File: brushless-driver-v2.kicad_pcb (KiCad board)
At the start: 2 copper layers, 86.5 x 63 mm, 37 parts, among them J1 Conn_01x07_Socket, J2 encoder, J3 motor, U5 L7805

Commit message: Started on second power stage, broke first power stage
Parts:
- added C12: 100n, Capacitor_SMD:C_0805_2012Metric_Pad1.18x1.45mm_HandSolder, F.Cu at (247.3, 37.5)
- added C13: 100n, Capacitor_SMD:C_0805_2012Metric_Pad1.18x1.45mm_HandSolder, F.Cu at (247.3, 40.5)
- added C14: 100n, Capacitor_SMD:C_0805_2012Metric_Pad1.18x1.45mm_HandSolder, F.Cu at (247.3, 43.5)
- added IC_A2: IFX007T, meiBib:TO-263-7_TabPin4, F.Cu at (142.5, 38.3)
- added IC_B2: IFX007T, meiBib:TO-263-7_TabPin4, F.Cu at (142.5, 50.6)
- added IC_C2: IFX007T, meiBib:TO-263-7_TabPin4, F.Cu at (142.5, 63.0)
- added J4: motor, TerminalBlock:TerminalBlock_MaiXu_MX126-5.0-03P_1x03_P5.00mm, F.Cu at (234.7, 30.9)
- added R13: 10k, Resistor_SMD:R_0805_2012Metric_Pad1.20x1.40mm_HandSolder, F.Cu at (233.0, 37.5)
- added R14: 10k, Resistor_SMD:R_0805_2012Metric_Pad1.20x1.40mm_HandSolder, F.Cu at (233.0, 40.5)
- added R15: 10k, Resistor_SMD:R_0805_2012Metric_Pad1.20x1.40mm_HandSolder, F.Cu at (233.0, 43.4)
- added R16: 10k, Resistor_SMD:R_0805_2012Metric_Pad1.20x1.40mm_HandSolder, F.Cu at (233.0, 46.4)
- added R17: 5k6, Resistor_SMD:R_0805_2012Metric_Pad1.20x1.40mm_HandSolder, F.Cu at (237.8, 37.5)
- added R18: 5k6, Resistor_SMD:R_0805_2012Metric_Pad1.20x1.40mm_HandSolder, F.Cu at (237.8, 40.5)
- added R19: 10k, Resistor_SMD:R_0805_2012Metric_Pad1.20x1.40mm_HandSolder, F.Cu at (237.8, 43.4)
- added R20: 10k, Resistor_SMD:R_0805_2012Metric_Pad1.20x1.40mm_HandSolder, F.Cu at (237.8, 46.4)
- added R21: 5k6, Resistor_SMD:R_0805_2012Metric_Pad1.20x1.40mm_HandSolder, F.Cu at (242.5, 37.5)
- added R22: 10k, Resistor_SMD:R_0805_2012Metric_Pad1.20x1.40mm_HandSolder, F.Cu at (242.5, 40.5)
- added R23: 10k, Resistor_SMD:R_0805_2012Metric_Pad1.20x1.40mm_HandSolder, F.Cu at (242.5, 43.4)
- added R24: 10k, Resistor_SMD:R_0805_2012Metric_Pad1.20x1.40mm_HandSolder, F.Cu at (242.5, 46.4)
- IC_A1, IC_B1, IC_C1: footprint myLib:PG-TO263-7-1 -> meiBib:TO-263-7_TabPin4
- J2: value encoder -> encoder_r
- moved R5 112.9 mm to (218.2, 37.5), turned to 0 degrees
- moved R6 112.1 mm to (218.2, 40.5), turned to 0 degrees
- moved R11 107.2 mm to (222.9, 43.4), turned to 0 degrees
- moved R12 106.5 mm to (222.9, 46.4), turned to 0 degrees
- moved R9 103.4 mm to (222.9, 37.5), turned to 0 degrees
- moved R10 102.7 mm to (222.9, 40.5), turned to 0 degrees
- moved C4 97.0 mm to (213.5, 52.3), turned to 0 degrees
- moved R3 96.6 mm to (213.4, 43.4), turned to 0 degrees
- moved R4 95.9 mm to (213.4, 46.4), turned to 0 degrees
- moved C3 91.1 mm to (213.5, 49.3), turned to 0 degrees
- moved R1 90.9 mm to (213.4, 37.5), turned to 0 degrees
- moved R2 90.2 mm to (213.4, 40.5), turned to 0 degrees
- moved R7 88.1 mm to (218.2, 43.4), turned to 0 degrees
- moved R8 85.3 mm to (218.2, 46.4), turned to 0 degrees
- moved C5 78.6 mm to (213.5, 55.4), turned to 0 degrees
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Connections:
- net DIR renamed DIR_R
- net EN renamed EN_R
- net HA renamed HA_R
- net HB renamed HB_R
- net HC renamed HC_R
- net THR renamed THR_R
- A1 pad 10: INH_B -> INH_B_R
- A1 pad 12: C -> C_R
- A1 pad 13: A -> A_R
- A1 pad 14: B -> B_R
- A1 pad 8: INH_C -> INH_C_R
- A1 pad 9: INH_A -> INH_A_R
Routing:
- net C_R: track 0.00 -> 32.1 mm, vias 0 -> 1
- net C: track 32.1 -> 0.00 mm, vias 1 -> 0
- net INH_C_R: track 0.00 -> 23.5 mm, vias 0 -> 1
- net INH_C: track 23.5 -> 0.00 mm, vias 1 -> 0
- net B: track 22.3 -> 0.00 mm, vias 1 -> 0
- net B_R: track 0.00 -> 22.3 mm, vias 0 -> 1
- net INH_A_R: track 0.00 -> 18.6 mm, vias 0 -> 2
- net INH_A: track 18.6 -> 0.00 mm, vias 2 -> 0
- net INH_B_R: track 0.00 -> 14.4 mm, vias 0 -> 1
- net INH_B: track 14.4 -> 0.00 mm, vias 1 -> 0
- net A_R: track 0.00 -> 11.8 mm, vias 0 -> 1
- net A: track 11.8 -> 0.00 mm, vias 1 -> 0
- net A_OUT: track 0.80 -> 0.27 mm

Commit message: zwischenspeichern
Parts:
- moved IC_A2 94.1 mm to (102.0, 123.2), turned to 180 degrees
- moved IC_B2 72.6 mm to (102.0, 110.8), turned to 180 degrees
- moved IC_C2 53.9 mm to (102.0, 98.5), turned to 180 degrees

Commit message: controller fw added, unfinished
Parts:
- removed A1: Arduino_Nano_v3.x, meiBib:Arduino_Nano
- removed D7: 5V6, meiBib:SOD-123W
- removed U5: L7805, meiBib:SOT-223-3_TabPin2
- added C15: 330n, Capacitor_SMD:C_0805_2012Metric_Pad1.18x1.45mm_HandSolder, F.Cu at (74.4, 76.2)
- added C16: 330p, Capacitor_SMD:C_0805_2012Metric_Pad1.18x1.45mm_HandSolder, F.Cu at (74.4, 79.2)
- added C17: 470u, Capacitor_THT:CP_Radial_D10.0mm_P5.00mm, F.Cu at (111.1, 38.0)
- added C18: 470u, Capacitor_THT:CP_Radial_D10.0mm_P5.00mm, F.Cu at (111.1, 49.5)
- added J5: encoder_l, Connector_JST:JST_PH_S5B-PH-K_1x05_P2.00mm_Horizontal, F.Cu at (82.5, 121.0)
- added U1: ESP32-WROOM-32E-R2, RF_Module:ESP32-WROOM-32D, F.Cu at (150.5, 129.0)
- added U2: ~, meiBib:TO-252-5-11, F.Cu at (134.0, 71.0)
- J3: value motor -> motor_R
- J4: value motor -> motor_L
- moved IC_A2 100.6 mm to (164.0, 44.0)
- moved IC_C2 100.6 mm to (164.0, 19.3)
- moved IC_B2 100.6 mm to (164.0, 31.6)
- moved C1 85.8 mm to (255.0, 84.5)
- moved C2 85.8 mm to (255.0, 81.5)
- moved C10 68.9 mm to (165.5, 65.0)
- moved C11 68.9 mm to (165.5, 67.5)
- moved C6 68.9 mm to (178.5, 65.0)
- moved C9 68.9 mm to (178.5, 67.5)
- moved C8 68.0 mm to (244.0, 79.1)
- moved H2 67.7 mm to (80.0, 90.0)
- moved H3 67.7 mm to (80.0, 140.0)
- moved C7 66.3 mm to (247.5, 98.1)
- moved PWR1 17.9 mm to (164.2, 89.5)
- moved J1 13.1 mm to (140.5, 91.5), turned to 180 degrees
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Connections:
- C6 pad 1: +5V -> +3V3
- C9 pad 1: +5V -> +3V3
- J1 pad 4: EN_R -> EN
- R10 pad 2: INH_B -> INH
- R11 pad 2: C -> C_R
- R12 pad 2: INH_C -> INH
- R14 pad 2: INH_C_L -> INH
- R16 pad 2: INH_B_L -> INH
- R20 pad 2: INH_A_L -> INH
- R7 pad 2: INH_A -> INH
- R8 pad 2: A -> A_R
- R9 pad 2: B -> B_R
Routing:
- net +5V: track 123.8 -> 0.00 mm
- net HB_R: track 80.6 -> 0.00 mm
- net HC_R: track 79.6 -> 0.00 mm, vias 1 -> 0
- net HA_R: track 76.7 -> 0.00 mm
- net VS: track 49.7 -> 0.00 mm, vias 36 -> 35
- net TX: track 34.7 -> 0.00 mm
- net EN_R: track 34.2 -> 0.00 mm
- net C_R: track 32.1 -> 0.00 mm, vias 1 -> 0
- net RX: track 31.7 -> 0.00 mm
- net INH_C_R: track 23.5 -> 0.00 mm, vias 1 -> 0
- net B_R: track 22.3 -> 0.00 mm, vias 1 -> 0
- net DIR_R: track 20.7 -> 0.00 mm
- net INH_A_R: track 18.6 -> 0.00 mm, vias 2 -> 0
- net INH_B_R: track 14.4 -> 0.00 mm, vias 1 -> 0
- net Net-(IC_B1-SR): track 12.1 -> 0.00 mm
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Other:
- board size 86.5 x 63 mm -> 152 x 60 mm

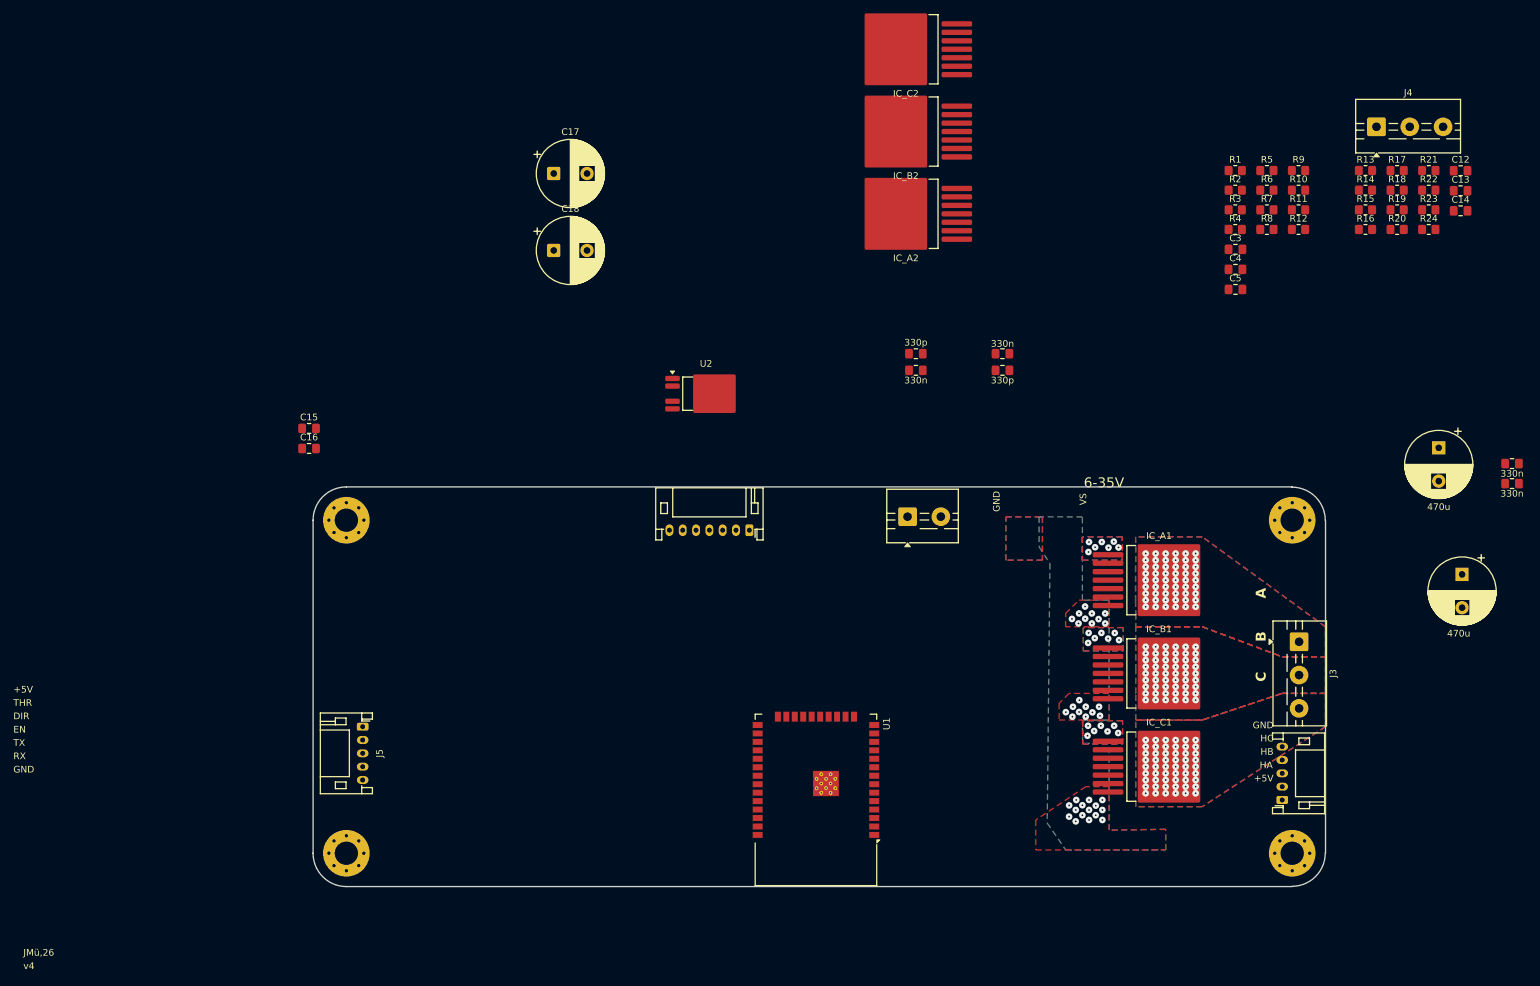
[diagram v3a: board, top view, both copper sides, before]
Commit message: added prg port for esp, started on pcb
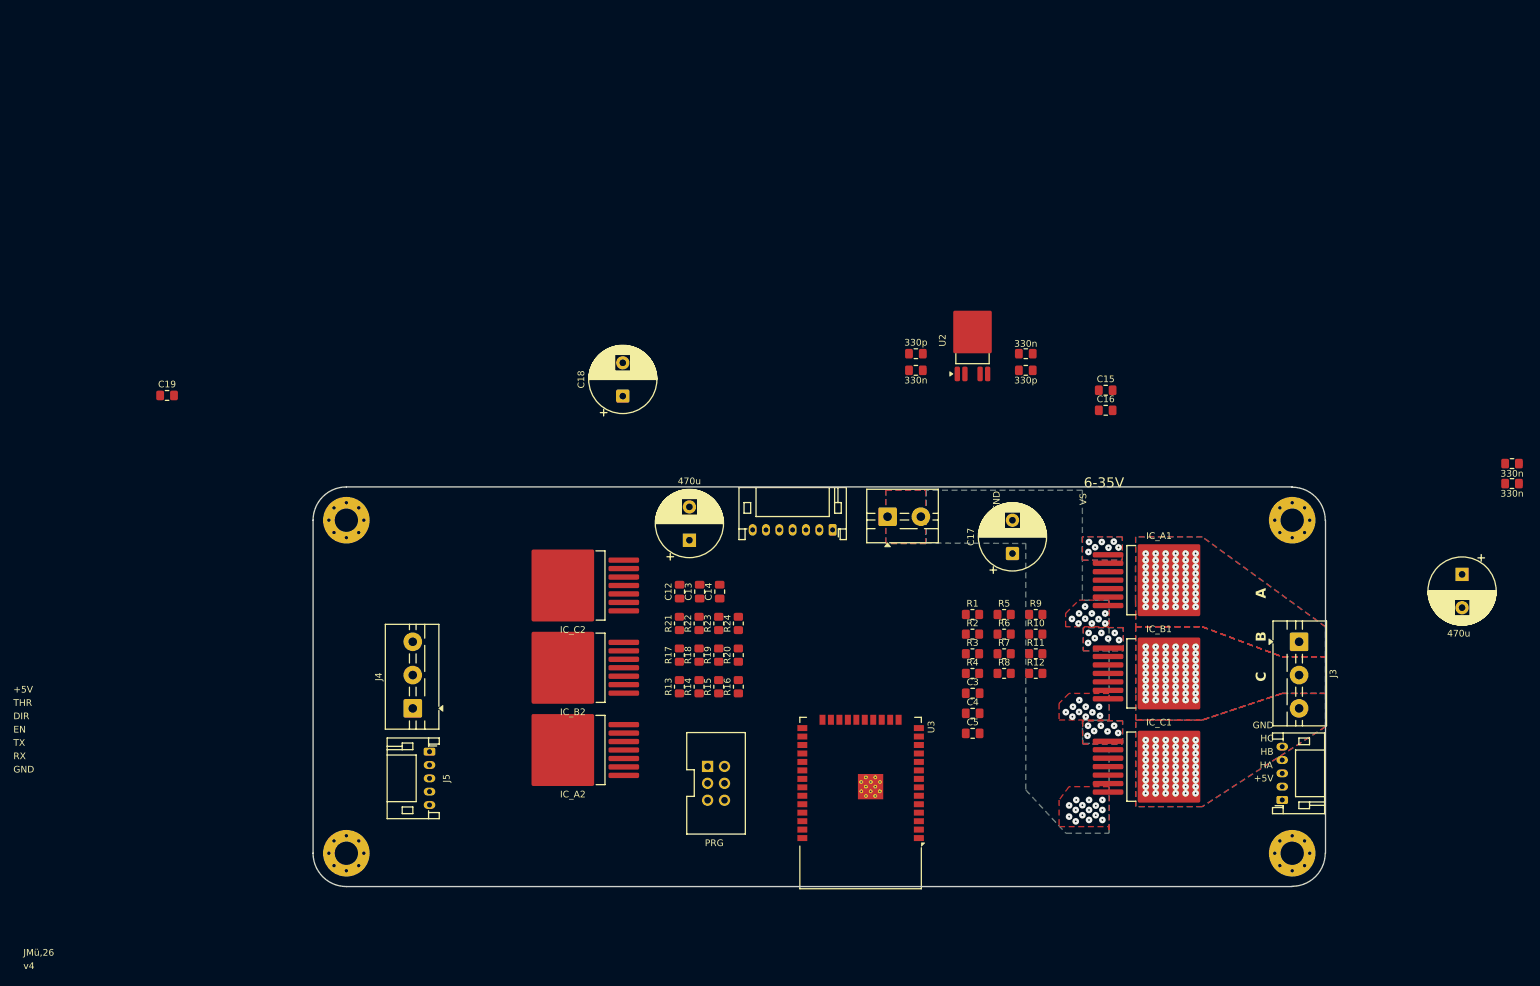
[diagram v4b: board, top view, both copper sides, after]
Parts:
- removed U1: ESP32-WROOM-32E-R2, RF_Module:ESP32-WROOM-32D
- added C19: 1uF, Capacitor_SMD:C_0805_2012Metric_Pad1.18x1.45mm_HandSolder, F.Cu at (53.1, 71.3)
- added J6: PRG, meiBib:Wannenstecker_6pin, F.Cu at (134.2, 127.0)
- added U3: ESP32-WROOM-32E, RF_Module:ESP32-WROOM-32D, F.Cu at (157.2, 129.5)
- moved J4 169.0 mm to (90.0, 118.2), turned to 90 degrees
- moved C12 133.2 mm to (130.0, 100.7), turned to 90 degrees
- moved R21 131.5 mm to (130.0, 105.5), turned to 90 degrees
- moved R17 130.0 mm to (130.0, 110.2), turned to 90 degrees
- moved C13 129.1 mm to (133.0, 100.7), turned to 90 degrees
- moved R13 128.9 mm to (130.0, 115.0), turned to 90 degrees
- moved R22 127.4 mm to (132.9, 105.5), turned to 90 degrees
- moved R18 125.9 mm to (132.9, 110.2), turned to 90 degrees
- moved C14 125.1 mm to (136.1, 100.7), turned to 90 degrees
- moved R14 124.8 mm to (132.9, 115.0), turned to 90 degrees
- moved R23 123.4 mm to (135.9, 105.5), turned to 90 degrees
- moved R19 121.8 mm to (135.9, 110.2), turned to 90 degrees
- moved R15 120.6 mm to (135.9, 115.0), turned to 90 degrees
- moved C15 119.7 mm to (194.0, 70.5)
- moved C16 119.7 mm to (194.0, 73.5)
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
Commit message: still unfinished
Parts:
- removed J1: Conn_01x07_Socket, Connector_JST:JST_PH_S7B-PH-K_1x07_P2.00mm_Horizontal
- added J7: ext-if, meiBib:Wannenstecker_10pin, F.Cu at (144.5, 110.3)
- added R25: 10k, Resistor_SMD:R_0805_2012Metric_Pad1.20x1.40mm_HandSolder, F.Cu at (171.5, 135.5)
- J6: value PRG -> prg
- moved C19 136.5 mm to (173.5, 135.5), turned to -90 degrees
- moved C7 111.9 mm to (136.0, 88.6)
- moved C2 97.2 mm to (159.5, 99.5), turned to -90 degrees
- moved C1 94.2 mm to (162.0, 99.5), turned to -90 degrees
- moved C6 51.9 mm to (170.0, 115.5), turned to -90 degrees
- moved C15 50.4 mm to (164.0, 111.0), turned to 180 degrees
- moved C9 50.1 mm to (167.5, 115.5), turned to -90 degrees
- moved C8 49.7 mm to (181.0, 88.6), turned to -90 degrees
- moved C16 46.5 mm to (164.0, 109.0), turned to 180 degrees
- moved U2 46.0 mm to (173.5, 109.0), turned to 0 degrees
- moved C10 34.5 mm to (164.5, 99.5), turned to -90 degrees
- moved C11 32.0 mm to (167.0, 99.5), turned to -90 degrees
- moved C18 30.8 mm to (147.0, 88.6), turned to -90 degrees
- moved R6 20.2 mm to (187.0, 125.5), turned to 180 degrees
- moved R5 20.1 mm to (182.0, 124.0), turned to 180 degrees
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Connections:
- U3 pad 11: A_R -> B_R
- U3 pad 12: B_R -> A_R
- U3 pad 13: EN -> unconnected-(U3-IO14-Pad13)
- U3 pad 14: DIR_L -> THR_L
- U3 pad 16: THR_L -> DIR_L
- U3 pad 27: unconnected-(U3-IO16-Pad27) -> THR_R
- U3 pad 28: HA_R -> EN
- U3 pad 29: THR_R -> C_L
- U3 pad 30: HB_R -> B_L
- U3 pad 31: HC_R -> A_L
- U3 pad 6: B_L -> HA_R
- U3 pad 7: C_L -> HB_R
- U3 pad 8: C_R -> HC_R
- U3 pad 9: A_L -> C_R
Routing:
- net INH: track 0.00 -> 59.7 mm, vias 0 -> 3
- net +3V3: track 0.00 -> 44.7 mm, vias 0 -> 2
- net RX: track 0.00 -> 30.1 mm
- net TX: track 0.00 -> 29.6 mm
- net RST: track 0.00 -> 17.6 mm
- net DIR_R: track 0.00 -> 17.1 mm, vias 0 -> 2
- net Net-(IC_C2-SR): track 0.00 -> 16.7 mm
- net Net-(IC_B2-SR): track 0.00 -> 16.5 mm
- net Net-(IC_C2-IN): track 0.00 -> 15.8 mm
- net Net-(IC_A2-SR): track 0.00 -> 15.3 mm
- net IO0: track 0.00 -> 13.5 mm
- net Net-(IC_B2-IN): track 0.00 -> 13.4 mm
- net Net-(IC_B2-INH): track 0.00 -> 8.21 mm
- net Net-(IC_B2-IS): track 0.00 -> 8.13 mm
- net +5V: track 0.00 -> 7.67 mm
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- added copper zone on B.Cu, net A_OUT_L
- added copper zone on F.Cu, net A_OUT_L
- added copper zone on B.Cu, net B_OUT_L
- added copper zone on F.Cu, net B_OUT_L
- added copper zone on B.Cu, net C_OUT_L
- added copper zone on F.Cu, net C_OUT_L
- removed copper zone on B.Cu, net VS
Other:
- copper layers 2 -> 4
- board text added: "motor_R"

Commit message: still wip
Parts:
- moved U2 9.33 mm to (165.0, 105.2), turned to 90 degrees
- moved C1 7.50 mm to (154.5, 99.5)
- moved C10 7.50 mm to (157.0, 99.5)
- moved C11 7.50 mm to (159.5, 99.5)
- moved C2 7.50 mm to (152.0, 99.5)
- moved H2 7.00 mm to (92.0, 90.0)
- moved H3 7.00 mm to (92.0, 140.0)
- moved C16 5.22 mm to (162.5, 114.0), turned to -90 degrees
- moved J7 3.35 mm to (143.0, 113.3)
- moved C15 3.16 mm to (165.0, 114.0), turned to -90 degrees
- moved C6 1.80 mm to (171.0, 114.0)
- moved C9 1.80 mm to (168.5, 114.0)
- renumbered U3 to ESP32-WROOM
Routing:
- net +5V: track 7.67 -> 174.9 mm, vias 0 -> 3
- net HA_L: track 0.00 -> 62.7 mm, vias 0 -> 2
- net INH: track 59.7 -> 122.2 mm, vias 3 -> 8
- net HB_L: track 0.00 -> 60.7 mm
- net HC_L: track 0.00 -> 60.6 mm
- net HC_R: track 0.00 -> 56.5 mm
- net HB_R: track 0.00 -> 56.4 mm
- net HA_R: track 0.00 -> 56.3 mm
- net C_L: track 0.00 -> 44.2 mm, vias 0 -> 2
- net B_L: track 0.00 -> 33.9 mm, vias 0 -> 2
- net A_R: track 0.00 -> 33.4 mm
- net +3V3: track 44.7 -> 76.5 mm, vias 2 -> 3
- net B_R: track 0.00 -> 26.3 mm
- net A_L: track 0.00 -> 24.5 mm, vias 0 -> 2
- net THR_L: track 0.00 -> 21.2 mm, vias 0 -> 1
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- added copper zone on In2.Cu, net GND
- added copper zone on In1.Cu, net VS
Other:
- board size 152 x 60 mm -> 140 x 60 mm
- board text added: "v5"
- board text removed: "DIR"
- board text removed: "EN"
- board text removed: "RX"
- board text removed: "THR"
- board text removed: "TX"
- board text removed: "v4"

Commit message: pcb finished
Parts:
- moved C2 22.8 mm to (173.5, 107.0), turned to 0 degrees
- moved C1 19.7 mm to (173.5, 104.5), turned to 0 degrees
- moved C10 16.7 mm to (173.5, 102.0), turned to 0 degrees
- moved C11 14.0 mm to (173.5, 99.5), turned to 0 degrees
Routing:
- net +5V: track 174.9 -> 17.4 mm, vias 3 -> 5
- net Net-(IC_A2-IN): track 0.00 -> 11.7 mm
- net GND: track 0.00 -> 4.91 mm, vias 44 -> 55
- added copper zone on In2.Cu, net +5V
- removed copper zone on In2.Cu, net GND
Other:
- board text added: "€€€ :("
